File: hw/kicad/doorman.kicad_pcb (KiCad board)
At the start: 2 copper layers, 28 x 80 mm, 20 parts, among them J1 Ring Detection, J2 Lock, J3 Power Supply, K1 S1A05, Q1 BC337, SW1 Button, U1 WeMos_D1_mini, U2 PC817

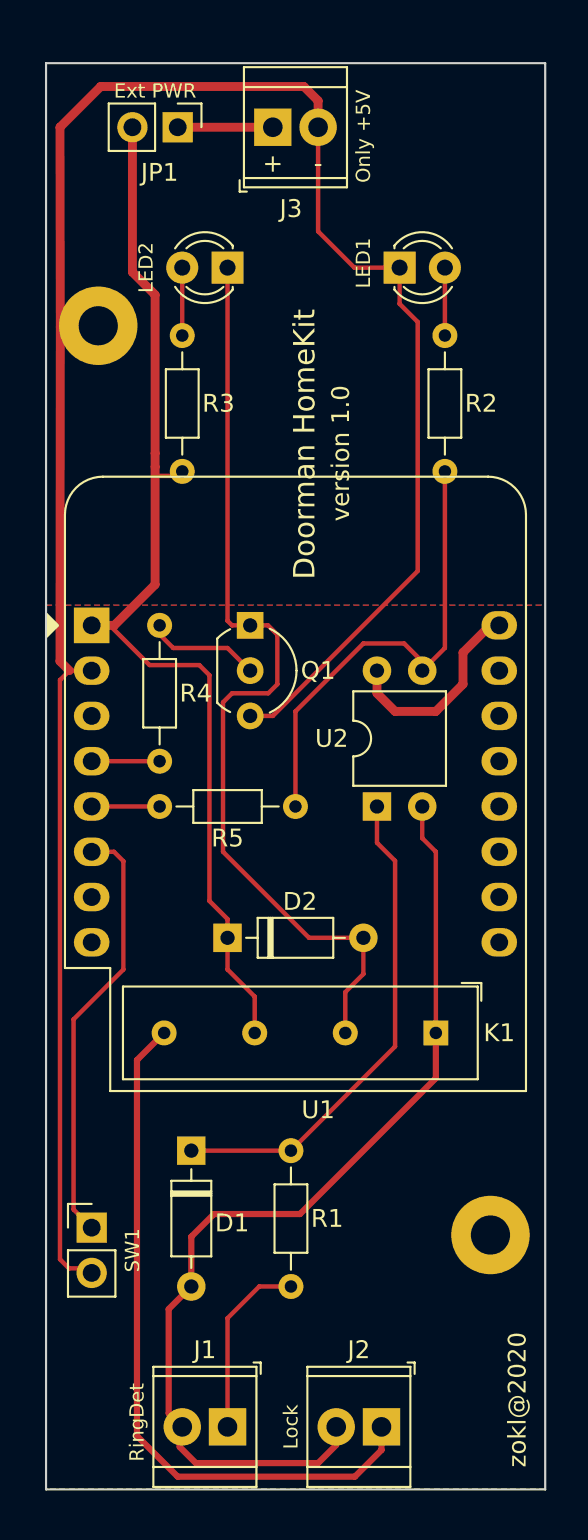
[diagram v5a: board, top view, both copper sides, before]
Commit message: First relase of redesign PCB because of wrong ESP module layout. Partialy fix #2
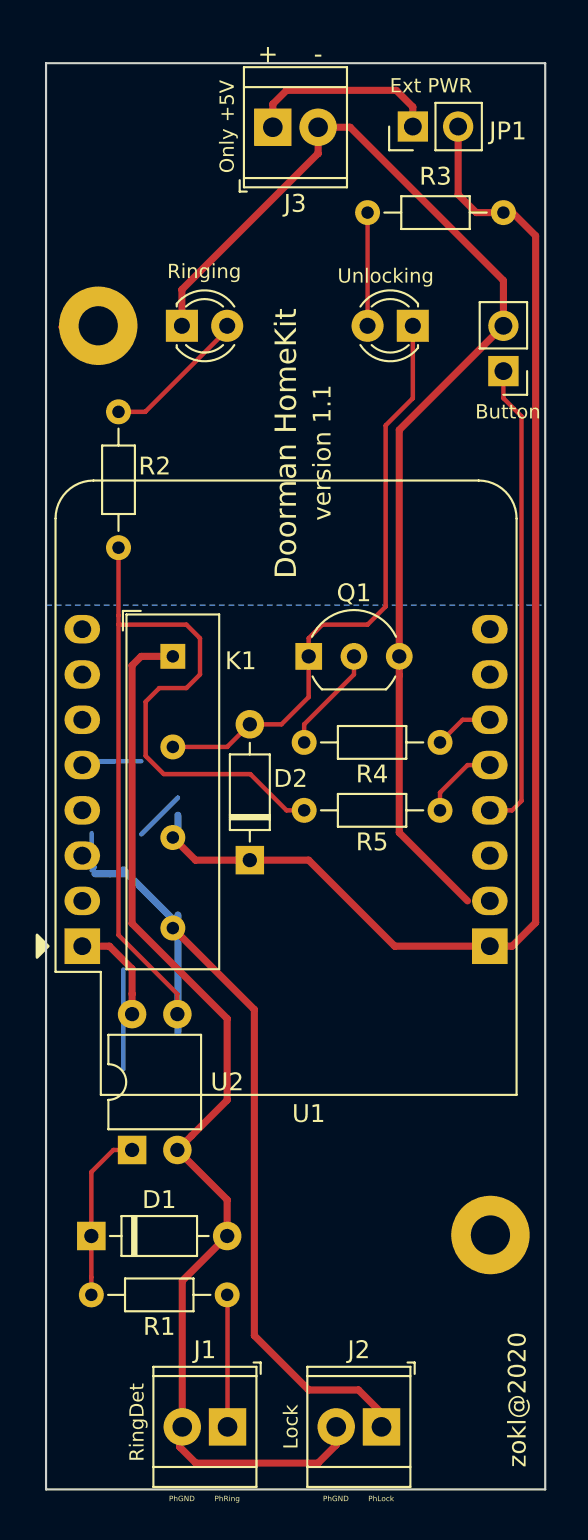
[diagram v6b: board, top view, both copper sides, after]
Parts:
- removed SW1: Button, Connector_PinHeader_2.54mm:PinHeader_1x02_P2.54mm_Vertical
- added Button: Button, Connector_PinHeader_2.54mm:PinHeader_1x02_P2.54mm_Vertical, F.Cu at (126.7, 68.5)
- U1: value WeMos_D1_mini -> WeMos_mini
- moved K1 25.8 mm to (108.2, 84.5), turned to 270 degrees
- moved U2 23.7 mm to (105.9, 112.2)
- moved R2 18.8 mm to (105.1, 70.8)
- moved JP1 13.2 mm to (121.6, 54.8), turned to 90 degrees
- moved Ringing 12.6 mm to (108.7, 66.0)
- moved R3 12.5 mm to (119.1, 59.7), turned to 0 degrees
- moved Unlocking 10.9 mm to (121.6, 66.0)
- moved R4 10.4 mm to (115.5, 89.4), turned to 0 degrees
- moved D1 7.37 mm to (103.6, 117.1), turned to 0 degrees
- moved D2 4.53 mm to (112.5, 96.0), turned to 90 degrees
- moved Q1 3.71 mm to (115.8, 84.5), turned to 0 degrees
- moved R1 3.61 mm to (111.2, 120.4), turned to 180 degrees
- moved U1 0.57 mm to (103.1, 83.0)
- moved R5 0.53 mm to (115.5, 93.2), turned to 0 degrees
- renumbered LED1 to Ringing, LED2 to Unlocking
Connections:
- R2 pad 2: Net-(R2-Pad2) -> PhLock
- R5 pad 1: Net-(R2-Pad2) -> PhLock
- U1 pad 10: Net-(U1-Pad10) -> (no net)
- U1 pad 11: Net-(U1-Pad11) -> (no net)
- U1 pad 12: Net-(U1-Pad12) -> (no net)
- U1 pad 13: Net-(U1-Pad13) -> (no net)
- U1 pad 14: Net-(U1-Pad14) -> (no net)
- U1 pad 15: Net-(U1-Pad15) -> (no net)
- U1 pad 3: Net-(U1-Pad3) -> (no net)
- U1 pad 4: Lock -> Butt
- U1 pad 6: Butt -> Lock
- U1 pad 7: Net-(U1-Pad7) -> (no net)
- U1 pad 8: Net-(U1-Pad8) -> (no net)
- U1 pad 9: Net-(U1-Pad9) -> (no net)
- U2 pad 3: Net-(R2-Pad2) -> PhLock
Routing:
- net PhLock: track 39.8 -> 98.9 mm
- net GND: track 128.1 -> 69.2 mm
- net Net-(R2-Pad2): track 26.7 -> 0.00 mm
- net Net-(D2-Pad2): track 53.2 -> 33.5 mm
- net Net-(D1-Pad1): track 27.7 -> 9.69 mm
- net +5V: track 61.7 -> 72.1 mm
- net Butt: track 24.1 -> 32.1 mm
- net PhGND: track 56.2 -> 62.5 mm
- net (no net): track 0.00 -> 6.00 mm
- net Net-(J3-Pad1): track 5.33 -> 11.0 mm
- net Net-(LED1-Pad2): track 3.81 -> 7.72 mm
- net PhRing: track 10.4 -> 7.41 mm
- net Net-(LED2-Pad2): track 3.81 -> 6.35 mm
- net RingDet: track 3.81 -> 4.43 mm
- removed copper zone on F.Cu, net GND
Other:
- board text added: "PhGND"
- board text added: "PhLock"
- board text added: "PhRing"
- board text added: "version 1.1"
- board text removed: "version 1.0"

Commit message: New PCB layout. Version 1.1.
Completly redesigned PCB layout. Fix of wrong Wemos D1 mini layout.
New antenna position and connectors to external LEDs and BUTTON.
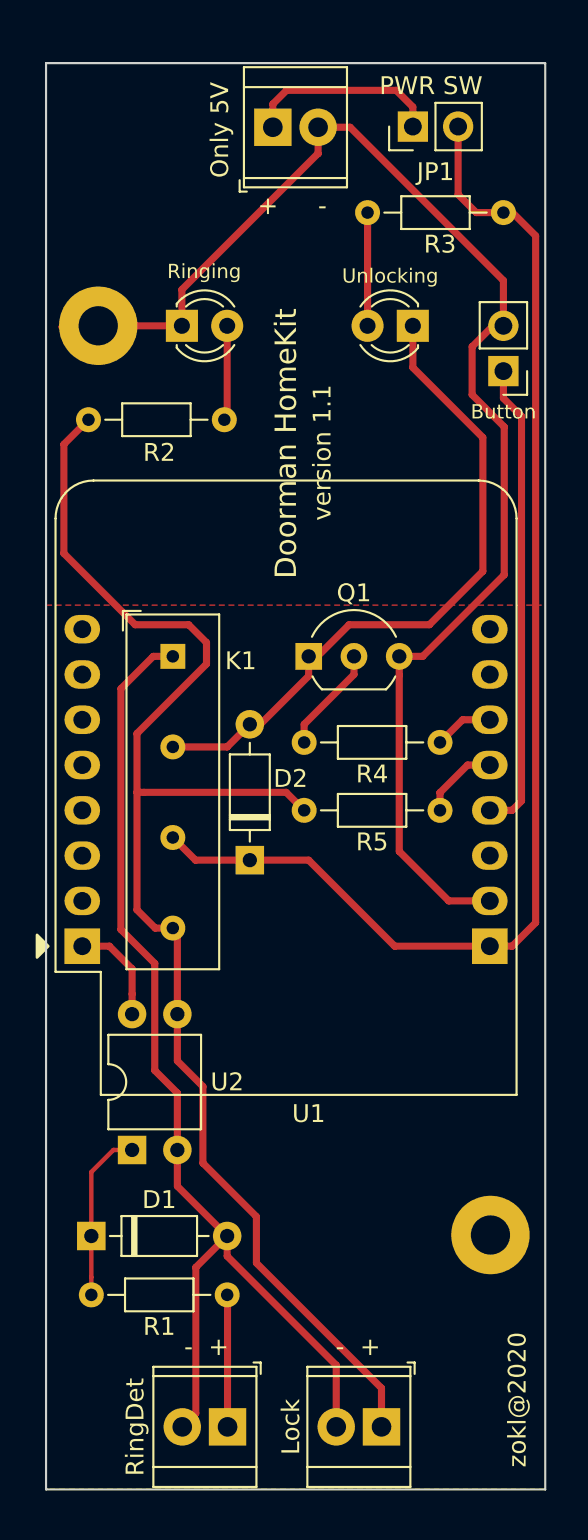
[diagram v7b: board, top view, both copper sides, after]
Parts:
- moved R2 5.95 mm to (111.1, 71.3), turned to 180 degrees
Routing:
- net PhLock: track 98.9 -> 79.8 mm
- net GND: track 69.2 -> 78.4 mm
- net (no net): track 6.00 -> 0.00 mm
- net +3V3: track 11.7 -> 5.86 mm
- net Butt: track 32.1 -> 26.5 mm
- net Net-(D2-Pad2): track 33.5 -> 37.5 mm
- net Net-(LED1-Pad2): track 7.72 -> 5.33 mm
- net +5V: track 72.1 -> 71.1 mm
- net PhGND: track 62.5 -> 61.8 mm
- added copper zone on F.Cu, net GND
- removed copper zone on B.Cu, net GND
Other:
- board text added: "- +"
- board text added: "Only 5V"
- board text added: "PWR SW"
- board text removed: "Ext PWR"
- board text removed: "Only +5V"
- board text removed: "PhGND"
- board text removed: "PhLock"
- board text removed: "PhRing"
